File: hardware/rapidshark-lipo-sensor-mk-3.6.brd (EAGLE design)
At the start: 30.5 x 17.8 mm, 26 parts, among them Q1 IRLML2244, Q2 IRLML2502, Q3 IRLML2244, Q4 IRLML2502, Q5 IRLML2244, Q6 IRLML2502, U1 Tiny84

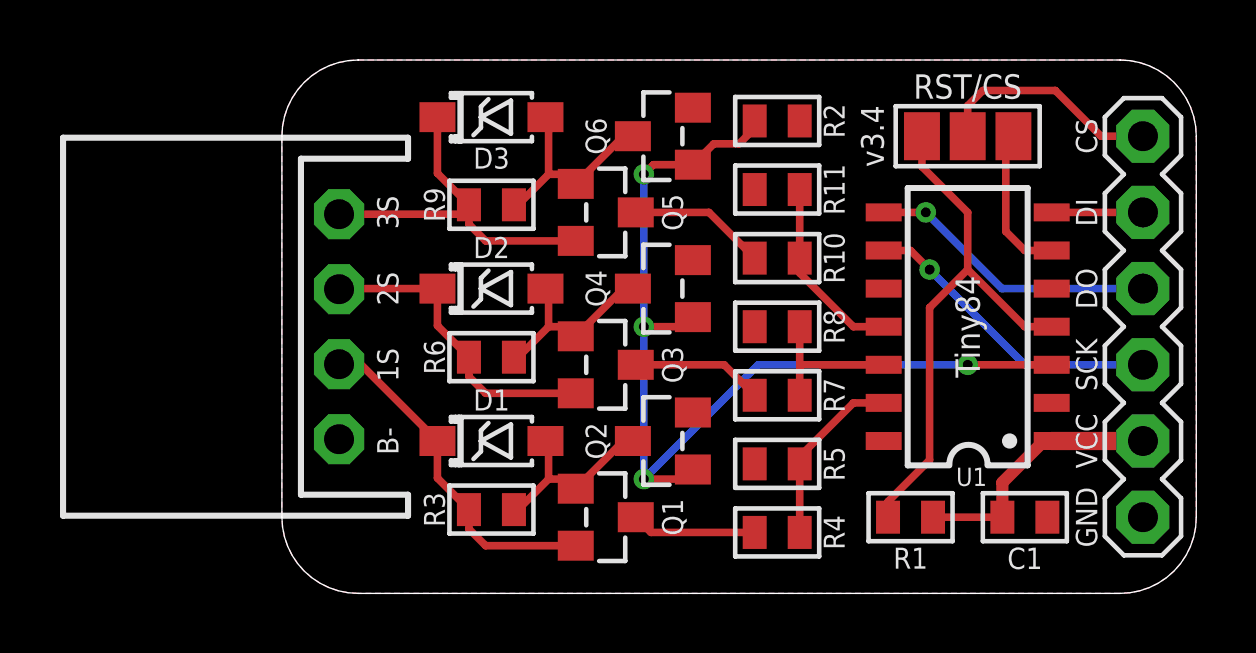
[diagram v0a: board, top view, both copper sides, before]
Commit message: lipo sensors suck
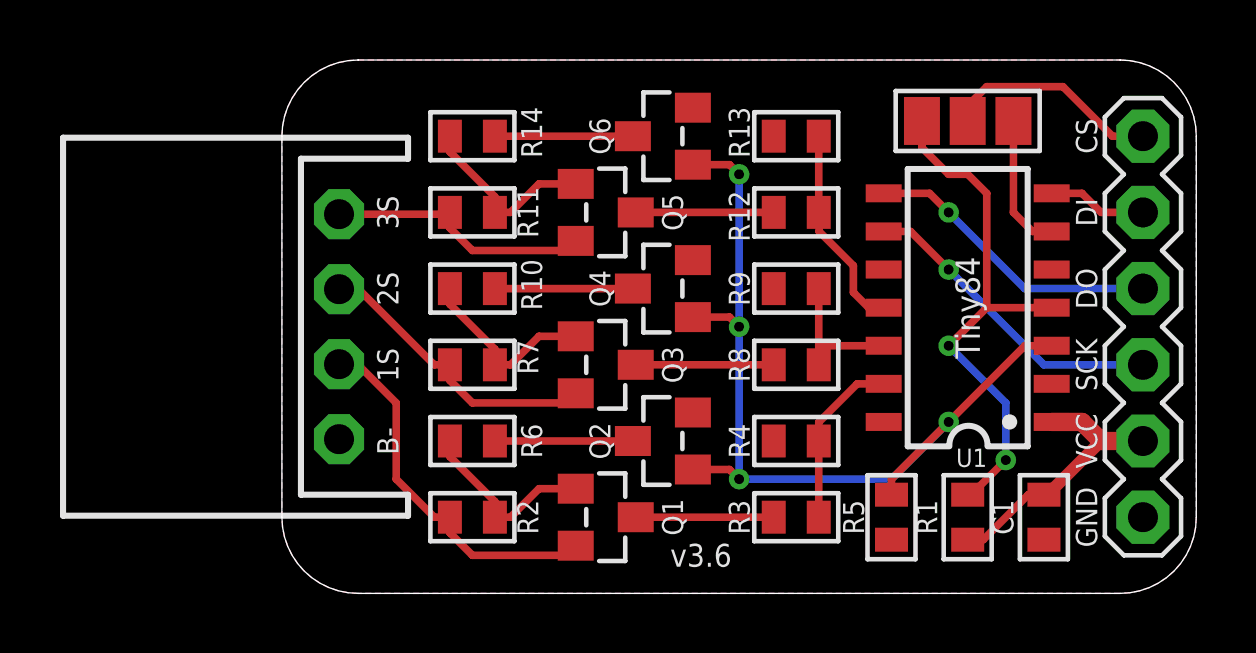
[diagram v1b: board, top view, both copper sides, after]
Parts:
- removed D1, D2, D3: MMSZ5240, a_parts:SOD123-ZENER
- added R12: 36K, a_parts:R0603-TIGHTER
- added R13: 10K, a_parts:R0603-TIGHTER
- added R14: 22K, a_parts:R0603-TIGHTER
- Q1, Q3, Q5: value IRLML2244 -> BSH203
- R10: value 36K -> 10K
- R2, R9: value 100K -> 10K
- R3: value 100K -> 4K7
- R4: value 4K7 -> 10K
- R6: value 100K -> 0R
- R7: value 22K -> 10K
- R8: value 10K -> 22K
- moved R2 16.7 mm to (6.35, 2.54), turned to 0 degrees
- moved R9 10.5 mm to (17.1, 10.2)
- moved R10 10.2 mm to (6.35, 10.2)
- moved R7 10.2 mm to (6.35, 7.62), turned to 0 degrees
- moved R11 10.2 mm to (6.35, 12.7)
- moved R3 10.2 mm to (17.1, 2.54), turned to 180 degrees
- moved R5 4.20 mm to (20.3, 2.54), turned to 90 degrees
- moved R4 3.11 mm to (17.1, 5.08), turned to 0 degrees
- moved R6 2.87 mm to (6.35, 5.08), turned to 180 degrees
- moved R1 1.91 mm to (22.9, 2.54), turned to 270 degrees
- moved R8 1.42 mm to (17.1, 7.62), turned to 180 degrees
- moved U1 0.63 mm to (22.9, 9.53)
- moved C1 0.63 mm to (25.4, 2.54), turned to 270 degrees
- moved RST/CS 0.51 mm to (22.9, 15.7)
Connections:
- new net N$1: Q4.3, R10.1
- new net N$8: Q6.3, R14.1
- new net N$9: Q2.3, R6.1
- net CELL1+: now also R2.1; no longer D1.C, R3.1
- net CELL2+: now also R7.1; no longer D2.C, R6.1
- net CELL3+: now also R11.1; no longer D3.C, R9.1
- net EN_DIV: now also R5.2; no longer R2.2
- net GND: now also R13.1, R4.1, R9.1; no longer R11.1, R2.1, R8.1
- net N$2: now also R8.2; no longer R7.2
- net N$3: now also R12.2; no longer R10.2
- net N$4: now also R2.2, R6.2; no longer D1.A, Q2.3, R3.2
- net N$5: now also R10.2, R7.2; no longer D2.A, Q4.3, R6.2
- net N$6: now also R3.2; no longer R4.2
- net N$7: now also R11.2, R14.2; no longer D3.A, Q6.3, R9.2
- net VDIV1: now also R3.1, R4.2; no longer R4.1, R5.2
- net VDIV2: now also R8.1, R9.2; no longer R7.1, R8.2
- net VDIV3: now also R12.1, R13.2; no longer R10.1, R11.2
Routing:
- net N$9: track 0.00 -> 4.60 mm
- net N$8: track 0.00 -> 4.60 mm
- net N$1: track 0.00 -> 4.60 mm
- net CELL3+: track 12.3 -> 8.88 mm
- net EN_DIV: track 33.4 -> 30.7 mm
- net CELL1+: track 11.5 -> 12.5 mm
- net N$7: track 7.13 -> 6.25 mm
- net VDIV3: track 6.32 -> 7.02 mm
- net CELL2+: track 10.4 -> 9.90 mm
- net RESET: track 18.0 -> 17.8 mm, vias 0 -> 2
